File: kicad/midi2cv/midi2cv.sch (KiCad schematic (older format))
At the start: 35 parts, among them J1 ProgramJmpr, J10 CTL1 Output, J11 CTL2 Output, J12 Gate1 Output, J13 Gate2 Output, J2 Power, J3 Conn_01x04_Male, J4 Conn_01x04_Female, J5 Conn_01x08_Male, J6 Conn_01x08_Female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

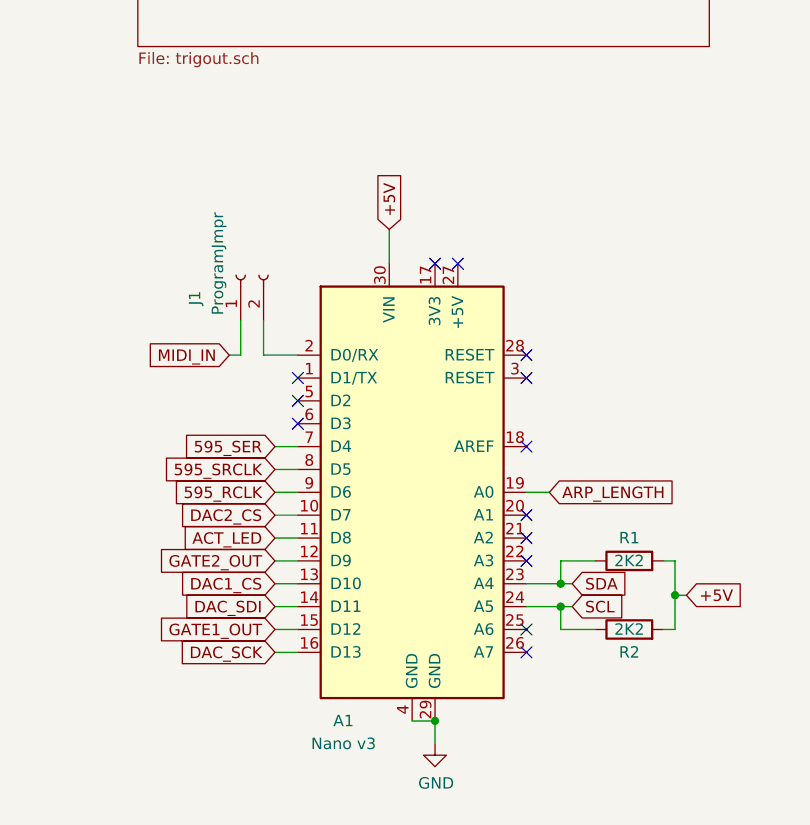
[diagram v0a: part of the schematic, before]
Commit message: Update some symbols + footprints.
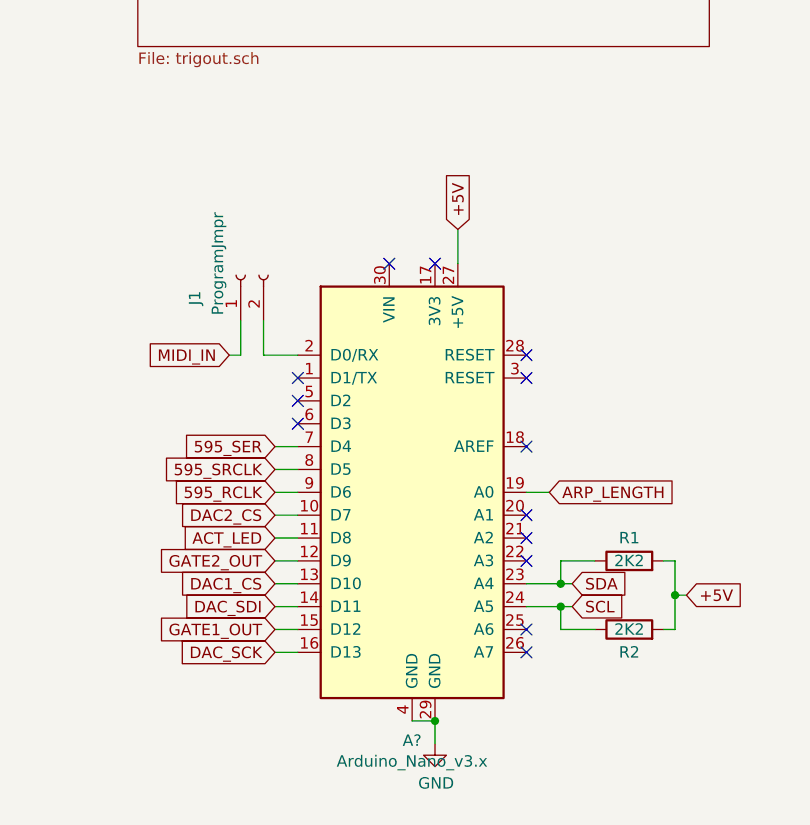
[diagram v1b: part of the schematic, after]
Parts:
- removed A1: Nano v3, Module:Arduino_Nano, symbol MCU_Module:Arduino_Nano_v3.x
- added A?: Arduino_Nano_v3.x, Module:Arduino_Nano, symbol Tomarus:Arduino_Nano_v3.x
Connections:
- net +5V: now also A?.27 (+5V)
- net 595_RCLK: now also A?.9 (D6)
- net 595_SER: now also A?.7 (D4)
- net 595_SRCLK: now also A?.8 (D5)
- net ACT_LED: now also A?.11 (D8)
- net ARP_LENGTH: now also A?.19 (A0)
- net DAC1_CS: now also A?.13 (D10)
- net DAC2_CS: now also A?.10 (D7)
- net DAC_SCK: now also A?.16 (D13)
- net DAC_SDI: now also A?.14 (D11)
- net GATE1_OUT: now also A?.15 (D12)
- net GATE2_OUT: now also A?.12 (D9)
- net GND: now also A?.29 (GND), A?.4 (GND)
- net SCL: now also A?.24 (A5)
- net SDA: now also A?.23 (A4)
- net at J1.2 (Pin_2): now also A?.2 (D0/RX)
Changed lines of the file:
@@
 	2400 1100 2400 1200
-$Comp
-L MCU_Module:Arduino_Nano_v3.x A1
-U 1 1 5CCDABBC
-P 2550 6350
-F 0 "A1" H 2250 5350 50  0000 C CNN
-F 1 "Nano v3" H 2250 5250 50  0000 C CNN
-F 2 "Module:Arduino_Nano" H 2700 5400 50  0001 L CNN
-F 3 "http://www.mouser.com/pdfdocs/Gravitech_Arduino_Nano3_0.pdf" H 2550 5350 50  0001 C CNN
-	1    2550 6350
-	1    0    0    -1
-$EndComp
 $Comp
 L Regulator_Linear:L7805 U1
@@
 	4200 900  4400 900
 Connection ~ 4200 900
-Text GLabel 2450 5200 1    50   Input ~ 0
+Text GLabel 2750 5200 1    50   Input ~ 0
 +5V
 $Comp
@@
 Wire Wire Line
 	2650 7350 2650 7450
-Connection ~ 2650 7350
 Text GLabel 1750 5750 0    50   Input ~ 0
 MIDI_IN
@@
 	0    -1   -1   0
 $EndComp
-Wire Wire Line
-	2450 5200 2450 5350
-NoConn ~ 2750 5350
 $Comp
 L Device:R_POT RV1
@@
 	1    0    0    -1
 $EndComp
+$Comp
+L Tomarus:Arduino_Nano_v3.x A?
+U 1 1 5CE84812
+P 2550 6350
+F 0 "A?" H 2550 5264 50  0000 C CNN
+F 1 "Arduino_Nano_v3.x" H 2550 5173 50  0000 C CNN
+F 2 "Module:Arduino_Nano" H 2700 5400 50  0001 L CNN
+F 3 "http://www.mouser.com/pdfdocs/Gravitech_Arduino_Nano3_0.pdf" H 2550 5350 50  0001 C CNN
+	1    2550 6350
+	1    0    0    -1
+$EndComp
+Connection ~ 2650 7350
+Wire Wire Line
+	2750 5350 2750 5200
+NoConn ~ 2450 5350
 $EndSCHEMATC

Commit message: More test code.
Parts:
- R3: value 1K -> 10K
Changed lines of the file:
@@
 P 6600 1400
 F 0 "R3" V 6500 1400 50  0000 C CNN
-F 1 "1K" V 6600 1400 50  0000 C CNN
+F 1 "10K" V 6600 1400 50  0000 C CNN
 F 2 "Resistor_THT:R_Axial_DIN0207_L6.3mm_D2.5mm_P7.62mm_Horizontal" V 6530 1400 50  0001 C CNN
 F 3 "~" H 6600 1400 50  0001 C CNN

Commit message: Fix caps silkscreen + powerconnector.
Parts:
- A1: renamed from A?; footprint Module:Arduino_Nano -> Tomarus:Arduino_Nano_Silk
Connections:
- net +12V: now also J2.10 (Pin_10), J2.9 (Pin_9); no longer J2.1 (Pin_1), J2.2 (Pin_2)
- net -12V: now also J2.1 (Pin_1), J2.2 (Pin_2); no longer J2.10 (Pin_10), J2.9 (Pin_9)
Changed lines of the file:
@@
 L Connector_Generic:Conn_02x05_Odd_Even J2
 U 1 1 5CCDA988
-P 2100 1100
-F 0 "J2" H 2150 1517 50  0000 C CNN
-F 1 "Power" H 2150 1426 50  0000 C CNN
-F 2 "Connector_IDC:IDC-Header_2x05_P2.54mm_Vertical" H 2100 1100 50  0001 C CNN
-F 3 "~" H 2100 1100 50  0001 C CNN
-	1    2100 1100
-	1    0    0    -1
+P 2200 1100
+F 0 "J2" H 2250 1517 50  0000 C CNN
+F 1 "Power" H 2250 1426 50  0000 C CNN
+F 2 "Connector_IDC:IDC-Header_2x05_P2.54mm_Vertical" H 2200 1100 50  0001 C CNN
+F 3 "~" H 2200 1100 50  0001 C CNN
+	1    2200 1100
+	-1   0    0    1
 $EndComp
 Wire Wire Line
@@
 $EndComp
 $Comp
-L Tomarus:Arduino_Nano_v3.x A?
+L Tomarus:Arduino_Nano_v3.x A1
 U 1 1 5CE84812
 P 2550 6350
-F 0 "A?" H 2550 5264 50  0000 C CNN
+F 0 "A1" H 2550 5264 50  0000 C CNN
 F 1 "Arduino_Nano_v3.x" H 2550 5173 50  0000 C CNN
-F 2 "Module:Arduino_Nano" H 2700 5400 50  0001 L CNN
+F 2 "Tomarus:Arduino_Nano_Silk" H 2700 5400 50  0001 L CNN
 F 3 "http://www.mouser.com/pdfdocs/Gravitech_Arduino_Nano3_0.pdf" H 2550 5350 50  0001 C CNN
 	1    2550 6350

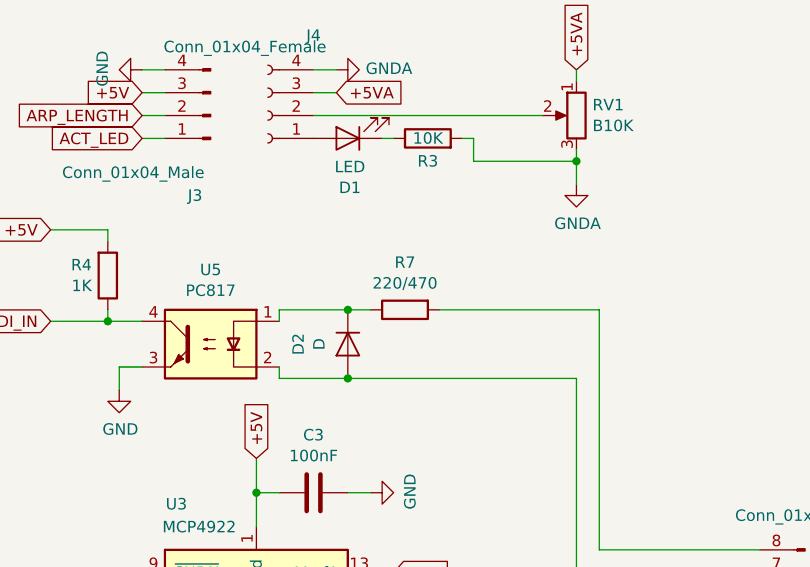
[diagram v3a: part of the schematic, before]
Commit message: Make trigger ports configurable as either drum trigger or clock divider.
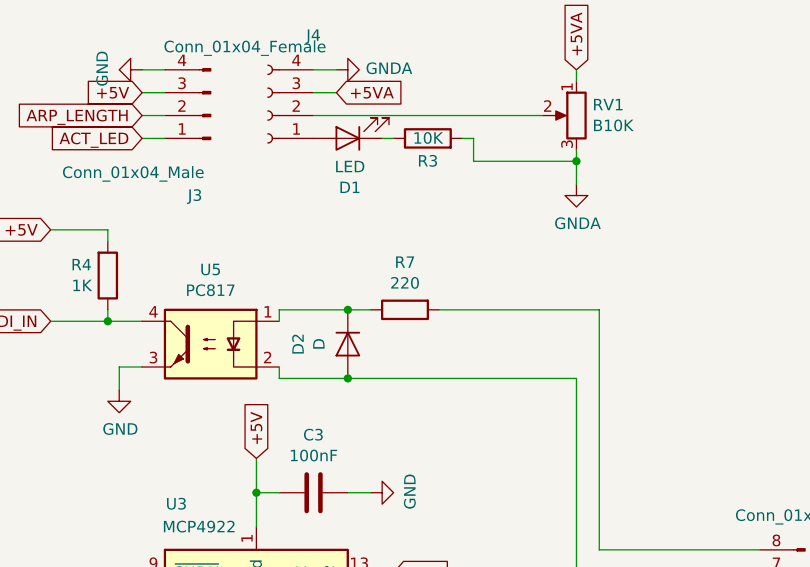
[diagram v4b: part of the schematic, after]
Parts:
- R7: value 220/470 -> 220
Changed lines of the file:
@@
 P 6500 2150
 F 0 "R7" V 6293 2150 50  0000 C CNN
-F 1 "220/470" V 6384 2150 50  0000 C CNN
+F 1 "220" V 6384 2150 50  0000 C CNN
 F 2 "Resistor_THT:R_Axial_DIN0207_L6.3mm_D2.5mm_P7.62mm_Horizontal" V 6430 2150 50  0001 C CNN
 F 3 "~" H 6500 2150 50  0001 C CNN
